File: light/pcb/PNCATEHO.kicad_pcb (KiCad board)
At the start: 2 copper layers, 85.6 x 54 mm, 49 parts, among them J1 USB_C_Receptacle_USB2.0, SW11 Boot, SW12 Reset, U1 RP2040, U2 RT9013-33GB, U3 W25Q32JVSSIQ, Y1 12MHz

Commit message: add esd protection
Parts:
- added TP4: 3.3, PNCATEHO:TestPoint_Pad_D2.0mm, F.Cu at (195.9, 111.3)
- added U4: USBLC6-2SC6, PNCATEHO:SOT-23-6_Handsoldering_REV, F.Cu at (193.0, 103.5)
- moved C2 67.1 mm to (187.5, 94.5)
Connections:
- J1 pad A6: USB_D+ -> USBBP
- J1 pad A7: USB_D- -> USBBN
- J1 pad B6: USB_D+ -> USBBP
- J1 pad B7: USB_D- -> USBBN
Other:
- board text added: "GB LIMITED EDITION"
- board text added: "inspired by aroum's r original design"
- board text added: "pncatehor welcome v0.1.5"
- board text removed: "inspired by aroum's original design"
- board text removed: "pncateho welcome v0.1"

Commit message: add some fix
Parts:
- moved TP4 5.95 mm to (190.8, 108.4)
- moved U4 1.35 mm to (192.2, 104.5)

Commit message: remove reset button
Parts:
- removed SW12: Reset, PNCATEHO:SW_SMD_L4_W3_H1.5
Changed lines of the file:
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@@
-		)
-	)
-	(footprint "PNCATEHO:SW_SMD_L4_W3_H1.5"
-		(layer "F.Cu")
-		(at 177.3 100 -90)
-		(descr "SPST tactile switch, SMD, 2 pins, 4×3×1.5 mm")
-		(property "Reference" "SW12"
-			(at 0 -2.413 90)
-			(layer "F.Fab")
-			(effects
-				(font
-					(size 1 1)
-					(thickness 0.15)
-				)
-			)
-		)
-		(property "Value" "Reset"
-			(at 3.75 0 180)
-			(layer "F.SilkS")
-			(effects
-				(font
-					(size 0.5 0.5)
-					(thickness 0.125)
-				)
-			)
-		)
-		(property "Datasheet" ""
-			(at 0 0 90)
-			(layer "F.Fab")
-			(hide yes)
-			(effects
-				(font
-					(size 1.27 1.27)
-					(thickness 0.15)
-				)
-			)
-		)
-		(property "Description" "Momentary push button, 2 pins"
-			(at 0 0 90)
-			(layer "F.Fab")
-			(hide yes)
-			(effects
-				(font
-					(size 1.27 1.27)
-					(thickness 0.15)
-				)
-			)
-		)
-		(sheetname "/")
-		(sheetfile "PNCATEHO.kicad_sch")
-		(attr through_hole)
-		(fp_rect
-			(start -2 -1.5)
-			(end 2 1.5)
-			(stroke
-				(width 0.1)
-				(type solid)
-			)
-			(fill no)
-			(layer "F.Fab")
-		)
-		(pad "1" smd roundrect
-			(at -2.4 0 270)
-			(size 1.2 1.8)
-			(layers "F.Cu" "F.Mask" "F.Paste")
-			(roundrect_rratio 0.1666666667)
-			(net 2 "GND")
-			(pinfunction "1")
-			(pintype "passive")
-		)
-		(pad "2" smd roundrect
-			(at 2.4 0 270)
-			(size 1.2 1.8)
-			(layers "F.Cu" "F.Mask" "F.Paste")
-			(roundrect_rratio 0.1666666667)
-			(net 38 "~{RESET}")
-			(pinfunction "2")
-			(pintype "passive")
-		)
-		(embedded_fonts no)
-		(model "${KIPRJMOD}/lib/step/SW_SPST_B3U-1000P-B.step"
-			(offset
-				(xyz 0 0 0)
-			)
-			(scale
-				(xyz 1.333 1.2 1.25)
-			)
-			(rotate
-				(xyz 0 0 0)
-			)
 		)
 	)

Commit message: change design
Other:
- outline, holes or cut-outs redrawn
- board text added: "020"
- board text added: "28.08.2025"
- board text added: "original designer name: aroum's"
- board text added: "pcb by: turtle & inpdiy"
- board text removed: "GB LIMITED EDITION"
- board text removed: "inspired by aroum's r original design"
- board text removed: "pcb by: turtle & inpudiy"
- board text removed: "pncatehor welcome v0.1.5"

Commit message: change design
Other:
- board text added: "ORIGINAL DESIGNER: AROUM'S"
- board text added: "PCB DESIGN BY: TURTLE INPUDIY"
- board text added: "VER: 020"
- board text added: "Valid: 08.25"
- board text removed: "020"
- board text removed: "28.08.2025"
- board text removed: "original designer name: aroum's"

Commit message: remove led
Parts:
- removed D1: RED, PNCATEHO:LED_0805_2012Metric_Pad1.15x1.40mm_HandSolder
- removed D2: BLUE, PNCATEHO:LED_0805_2012Metric_Pad1.15x1.40mm_HandSolder
- removed R10, R9: 1k, PNCATEHO:R_0805_2012Metric_Pad1.20x1.40mm_HandSolder
- removed R8: 10k, PNCATEHO:R_0805_2012Metric_Pad1.20x1.40mm_HandSolder
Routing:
- net +3V3: track 189.9 -> 162.1 mm, vias 7 -> 5
- net STATE_LED: track 26.7 -> 0.00 mm
- net Net-(D2-K): track 10.8 -> 0.00 mm
- net Net-(D1-K): track 3.40 -> 0.00 mm

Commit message: fix
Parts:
- added D1: Red, PNCATEHO:D_0805_2012Metric_Pad1.15x1.40mm_HandSolder, F.Cu at (199.3, 108.9)
- added D2: Blue, PNCATEHO:D_0805_2012Metric_Pad1.15x1.40mm_HandSolder, F.Cu at (199.3, 112.0)
- added R10: 1k, PNCATEHO:R_0805_2012Metric_Pad1.20x1.40mm_HandSolder, F.Cu at (194.6, 114.8)
- added R8: 10k, PNCATEHO:R_0805_2012Metric_Pad1.20x1.40mm_HandSolder, F.Cu at (194.6, 108.9)
- added R9: 1k, PNCATEHO:R_0805_2012Metric_Pad1.20x1.40mm_HandSolder, F.Cu at (194.6, 111.8)
- added SW12: Boot, PNCATEHO:PADS, F.Cu at (199.3, 103.1)
- SW11: footprint PNCATEHO:SW_SMD_L4_W3_H1.5 -> PNCATEHO:PADS
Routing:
- net ~{RESET}: track 83.1 -> 72.3 mm

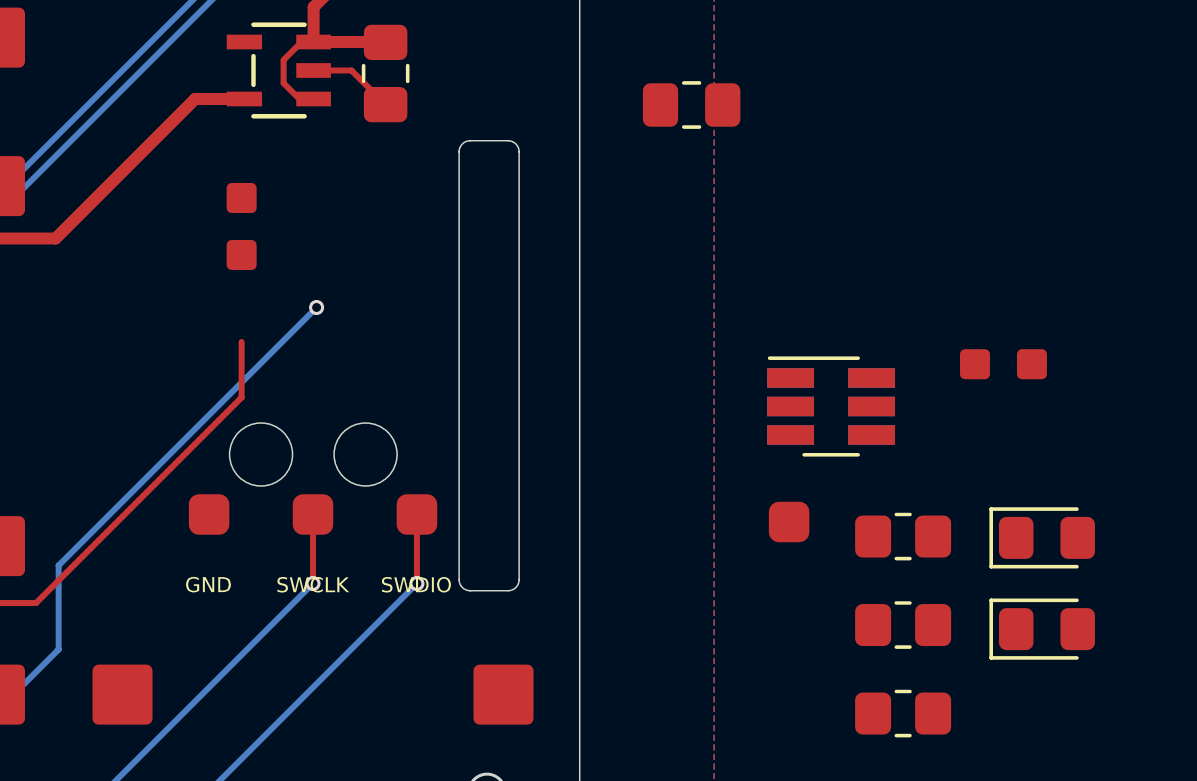
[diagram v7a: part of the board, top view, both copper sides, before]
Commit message: add button
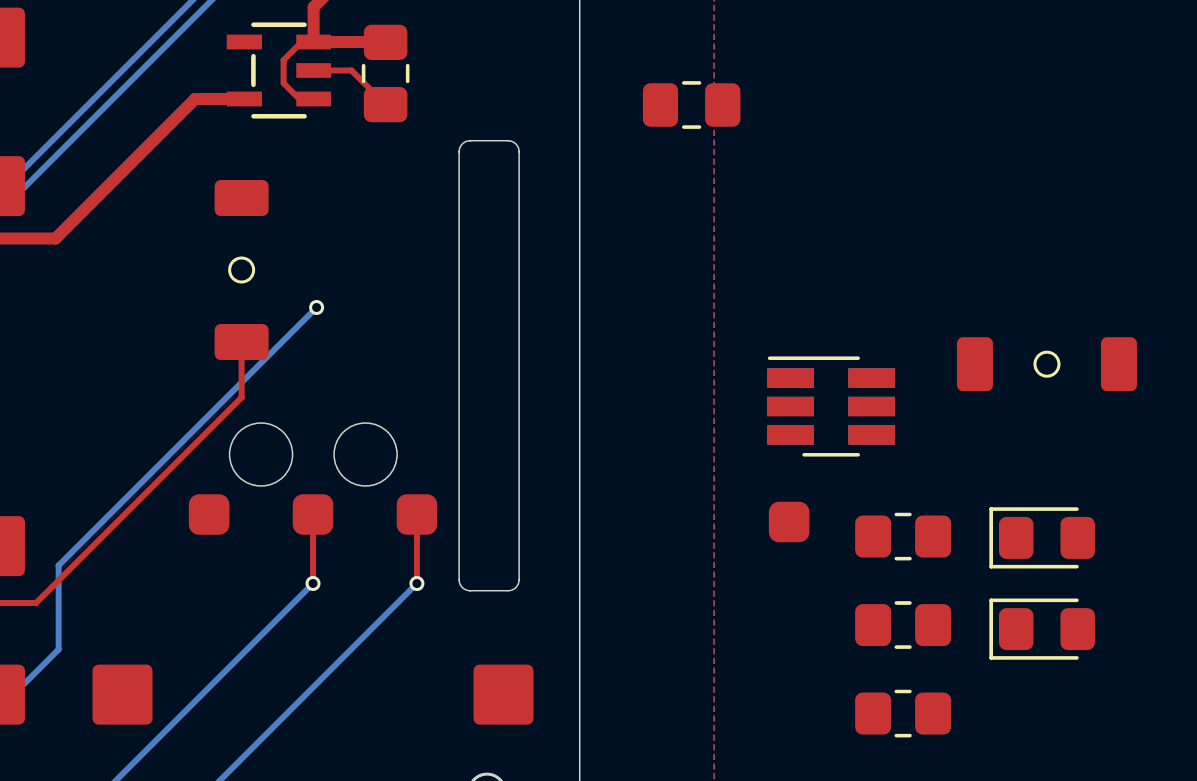
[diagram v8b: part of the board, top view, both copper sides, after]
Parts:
- SW11, SW12: footprint PNCATEHO:PADS -> PNCATEHO:SW_PUSH
